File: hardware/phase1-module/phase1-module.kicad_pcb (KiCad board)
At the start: 4 copper layers, 120 x 80 mm, 144 parts, among them J1 VBUS IN, J2 SWD, J3 UART, J4 OUTPUT, J5 BACKPLANE, J6 FAN, Q1 CSD18563Q5A, Q2 CSD18563Q5A, Q3 60V NFET, Q4 60V NFET, Q5 2N7002, Q6 2N7002, Q7 2N7002, Q8 2N7002, Q9 2N7002, U1 DAC80502DRXT, U10 STM32G431CBT6, U11 TCAN1042HGV, U2 OPA2333, U3 LM5145RGYR, U4 INA240A3, U5 INA228, U6 LTC7004, U7 TLV7011, U8 LMR36015AQRNXRQ1, U9 NCP1117-3.3, Y1 8MHz

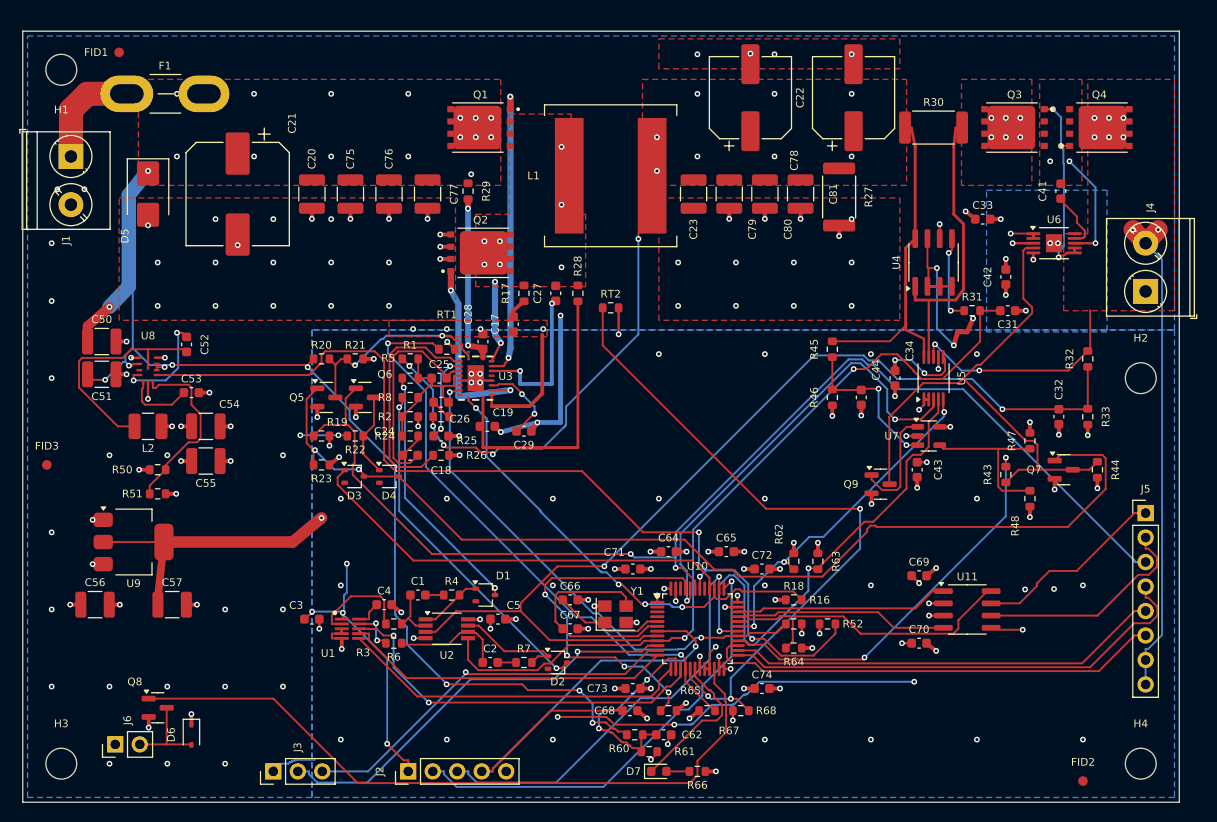
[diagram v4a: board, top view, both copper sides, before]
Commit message: Phase-1 100x80 (WIP): re-place output section around the 17 mm L1 land
Placement, pours and pass-1 copper for the 100 x 80 board; routing to follow.
Also corrects the Phase-1 F1 BOM note (direct-solder mini blade land).

Co-Authored-By: Claude Opus 5.5 (1M context) <noreply@anthropic.com>
Claude-Session: https://claude.ai/code/session_017ZrT5TjsLMQoxTZy1jabew
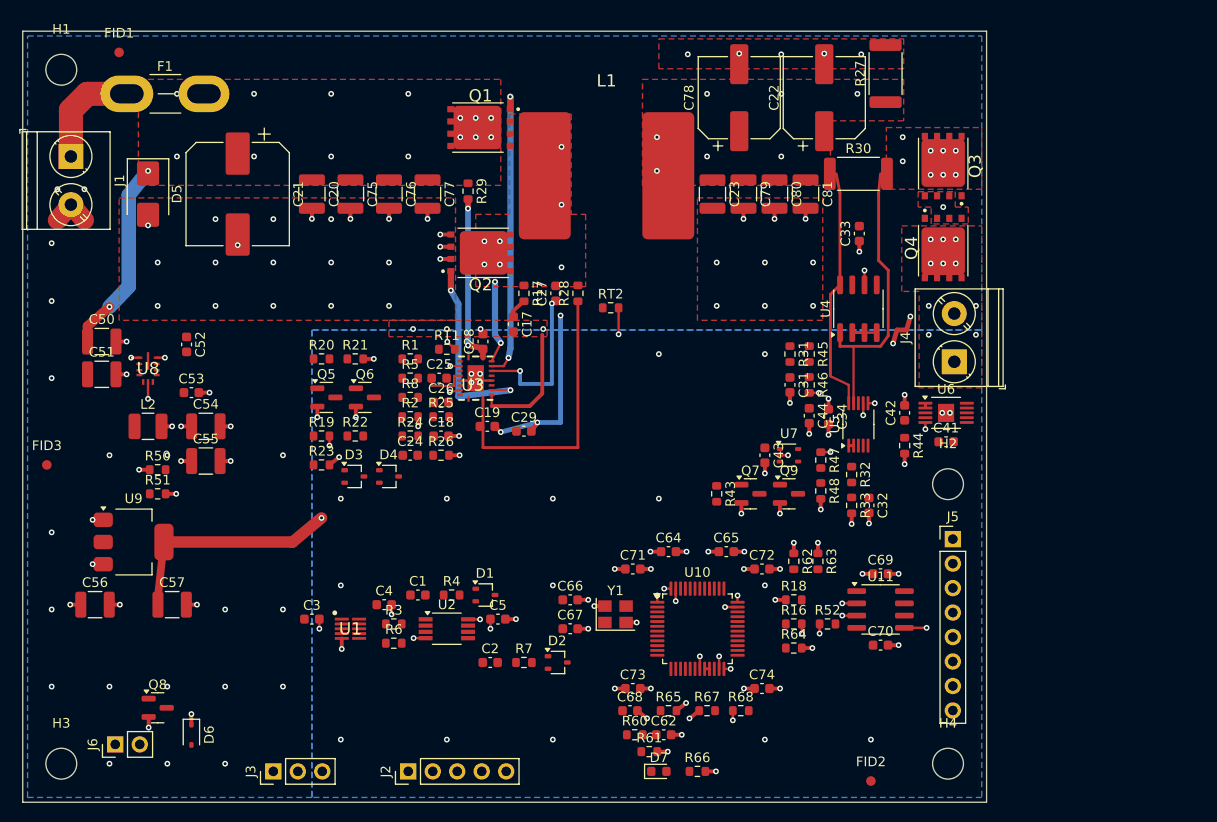
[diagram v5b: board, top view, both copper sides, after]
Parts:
- C1, C17, C18, C19, C2, C24, C25, C26, C27, C28, C29, C3, C31, C32, C33, C34, C4, C41, C42, C43, C44, C5, C52, C53, C62, C64, C65, C68, C69, C70, C71, C72, C73, C74: footprint Capacitor_SMD:C_0603_1608Metric -> C_0603_1608Metric
- C20, C23, C50, C51, C54, C55, C56, C57, C75, C76, C77, C79, C80, C81: footprint Capacitor_SMD:C_1210_3225Metric -> C_1210_3225Metric
- C21: footprint Capacitor_SMD:CP_Elec_10x10.5 -> CP_Elec_10x10.5
- C22, C78: footprint Capacitor_SMD:CP_Elec_8x11.9 -> CP_Elec_8x11.9
- C66, C67: value 10p -> 18p; footprint Capacitor_SMD:C_0603_1608Metric -> C_0603_1608Metric
- D1, D2, D3, D4: footprint Package_TO_SOT_SMD:SOT-323_SC-70 -> SOT-323_SC-70
- D5: footprint Diode_SMD:D_SMB -> D_SMB
- D6: footprint Diode_SMD:D_SOD-323 -> D_SOD-323
- D7: footprint LED_SMD:LED_0603_1608Metric -> LED_0603_1608Metric
- F1: footprint Fuse:Fuse_Blade_Mini_directSolder -> Fuse_Blade_Mini_directSolder
- FID1, FID2, FID3: footprint Fiducial:Fiducial_1mm_Mask2mm -> Fiducial_1mm_Mask2mm
- H1, H2, H3, H4: footprint MountingHole:MountingHole_3.2mm_M3 -> MountingHole_3.2mm_M3
- J1, J4: footprint TerminalBlock_Phoenix:TerminalBlock_Phoenix_PT-1,5-2-5.0-H_1x02_P5.00mm_Horizontal -> TerminalBlock_Phoenix_PT-1,5-2-5.0-H_1x02_P5.00mm_Horizontal
- J2: footprint Connector_PinHeader_2.54mm:PinHeader_1x05_P2.54mm_Vertical -> PinHeader_1x05_P2.54mm_Vertical
- J3: footprint Connector_PinHeader_2.54mm:PinHeader_1x03_P2.54mm_Vertical -> PinHeader_1x03_P2.54mm_Vertical
- J5: footprint Connector_PinHeader_2.54mm:PinHeader_1x08_P2.54mm_Vertical -> PinHeader_1x08_P2.54mm_Vertical
- J6: footprint Connector_PinHeader_2.54mm:PinHeader_1x02_P2.54mm_Vertical -> PinHeader_1x02_P2.54mm_Vertical
- L1: value XAL1350-103ME 10u/14A -> 10u MWSA1707S-100/XAL1350; footprint Inductor_SMD:L_Coilcraft_XAL1350-XXX -> L_1707_XAL1510
- L2: footprint Inductor_SMD:L_1210_3225Metric -> L_1210_3225Metric
- NT1: footprint NetTie:NetTie-2_SMD_Pad0.5mm -> NetTie-2_SMD_Pad0.5mm
- Q1, Q2, Q3, Q4: footprint labbench:PowerFET_SON5x6_GDS -> PowerFET_SON5x6_GDS
- Q5, Q6, Q7, Q8, Q9: footprint Package_TO_SOT_SMD:SOT-23 -> SOT-23
- R1, R16, R17, R18, R19, R2, R20, R21, R22, R23, R24, R25, R26, R28, R29, R3, R31, R32, R33, R4, R43, R44, R45, R46, R47, R48, R5, R50, R51, R52, R6, R60, R61, R62, R63, R64, R65, R66, R67, R68, R7, R8, RT1, RT2: footprint Resistor_SMD:R_0603_1608Metric -> R_0603_1608Metric
- R27, R30: footprint Resistor_SMD:R_2512_6332Metric -> R_2512_6332Metric
- U1: footprint labbench:DAC80502_DRX_WSON-10 -> DAC80502_DRX_WSON-10
- U10: footprint Package_QFP:LQFP-48_7x7mm_P0.5mm -> LQFP-48_7x7mm_P0.5mm
- U11, U4: footprint Package_SO:SOIC-8_3.9x4.9mm_P1.27mm -> SOIC-8_3.9x4.9mm_P1.27mm
- U2: footprint Package_SO:VSSOP-8_3.0x3.0mm_P0.65mm -> VSSOP-8_3.0x3.0mm_P0.65mm
- U3: footprint labbench:LM5145_RGY0020B -> LM5145_RGY0020B
- U5: footprint Package_SO:VSSOP-10_3x3mm_P0.5mm -> VSSOP-10_3x3mm_P0.5mm
- U6: footprint Package_SO:MSOP-10-1EP_3x3mm_P0.5mm_EP1.68x1.88mm -> MSOP-10-1EP_3x3mm_P0.5mm_EP1.68x1.88mm
- U7: value TLV7011 -> TLV7011DCK; footprint Package_TO_SOT_SMD:SOT-23-5 -> SOT-353_SC-70-5
- U8: footprint labbench:LMR36015_RNX_VQFN-HR-12 -> LMR36015_RNX_VQFN-HR-12
- U9: footprint Package_TO_SOT_SMD:SOT-223-3_TabPin2 -> SOT-223-3_TabPin2
- Y1: footprint Crystal:Crystal_SMD_3225-4Pin_3.2x2.5mm -> Crystal_SMD_3225-4Pin_3.2x2.5mm
- moved Q7 32.6 mm to (95.5, 68.0)
- moved R43 30.1 mm to (92.0, 68.0)
- moved C41 28.6 mm to (115.8, 62.6), turned to 0 degrees
- moved R32 27.3 mm to (106.0, 66.0)
- moved R33 26.2 mm to (106.0, 69.2)
- moved C31 23.9 mm to (99.6, 56.7), turned to -90 degrees
- moved H2 22.8 mm to (116.0, 67.0)
- moved FID2 22.0 mm to (108.0, 97.8)
- moved R47 21.8 mm to (102.8, 64.5)
- moved C32 21.7 mm to (107.8, 69.2)
- moved R48 21.7 mm to (102.8, 67.7)
- moved J4 21.1 mm to (116.7, 54.3)
- moved U6 20.9 mm to (115.8, 59.6)
- moved Q4 20.5 mm to (115.5, 42.5), turned to 90 degrees
- moved J5 20.2 mm to (116.5, 72.7)
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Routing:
- net HW_EN: track 122.9 -> 0.00 mm, vias 2 -> 0
- net EN_KILL: track 109.4 -> 0.00 mm, vias 2 -> 0
- net V_MEAS: track 103.4 -> 0.00 mm, vias 2 -> 0
- net AUX_PG: track 100.1 -> 0.00 mm, vias 3 -> 0
- net VBUS_F: track 117.4 -> 20.2 mm, vias 25 -> 16
- net I_MEAS: track 83.5 -> 0.00 mm, vias 2 -> 0
- net FAN_PWM: track 73.7 -> 0.00 mm
- net NTC_IND: track 71.3 -> 0.00 mm, vias 3 -> 0
- net NTC_FET: track 61.8 -> 0.00 mm, vias 2 -> 0
- net DISC_INP: track 57.8 -> 0.00 mm
- net VOUT_INT: track 82.5 -> 25.5 mm, vias 13 -> 7
- net I2C_SDA: track 52.1 -> 0.00 mm, vias 2 -> 0
- net PS_FPWM: track 52.8 -> 1.07 mm, vias 2 -> 1
- net NRST: track 50.2 -> 0.00 mm, vias 1 -> 0
- net SLOT_ID0: track 50.0 -> 0.00 mm
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- removed copper zone on In2.Cu, net DISC_SRC
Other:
- board size 120 x 80 mm -> 100 x 80 mm

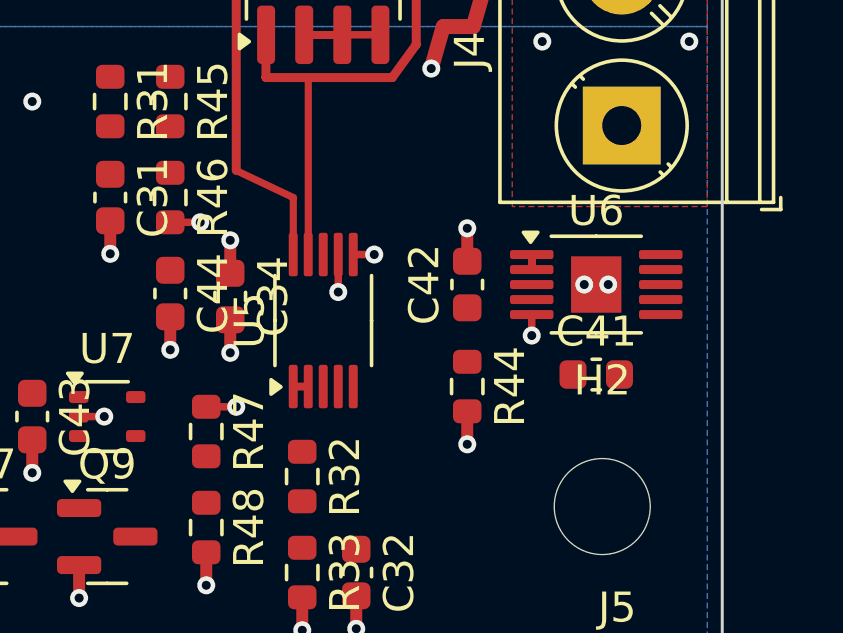
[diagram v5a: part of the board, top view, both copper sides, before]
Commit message: Phase-1 100x80 (WIP): turn U6 so gate/source/BST pins face their parts
Co-Authored-By: Claude Opus 5.5 (1M context) <noreply@anthropic.com>
Claude-Session: https://claude.ai/code/session_017ZrT5TjsLMQoxTZy1jabew
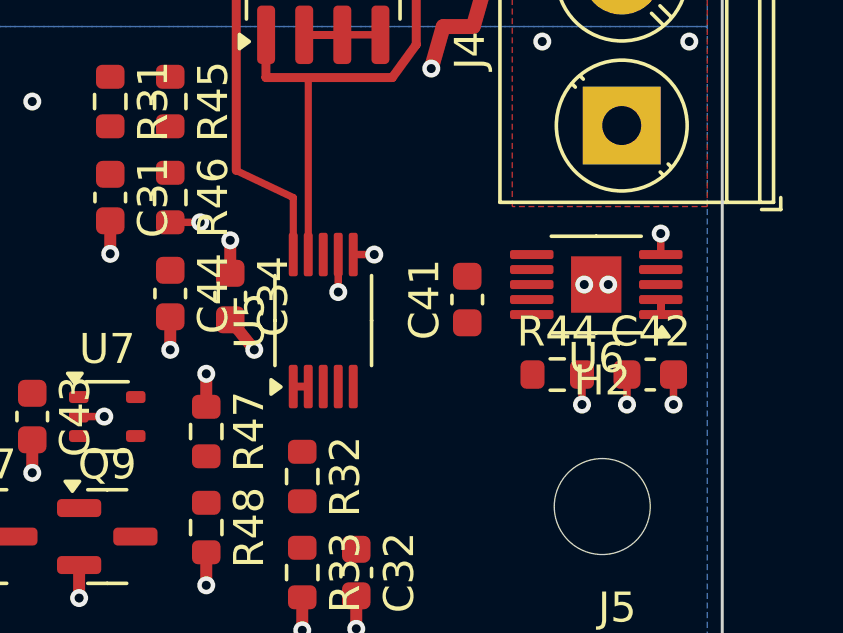
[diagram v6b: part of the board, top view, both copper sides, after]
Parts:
- moved C42 6.80 mm to (117.6, 62.6), turned to 0 degrees
- moved C41 4.97 mm to (111.5, 60.1), turned to 90 degrees
- moved R44 3.03 mm to (114.5, 62.6), turned to 0 degrees
- turned U6 to 180 degrees
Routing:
- net 5V0: track 16.1 -> 17.1 mm, vias 13 -> 14

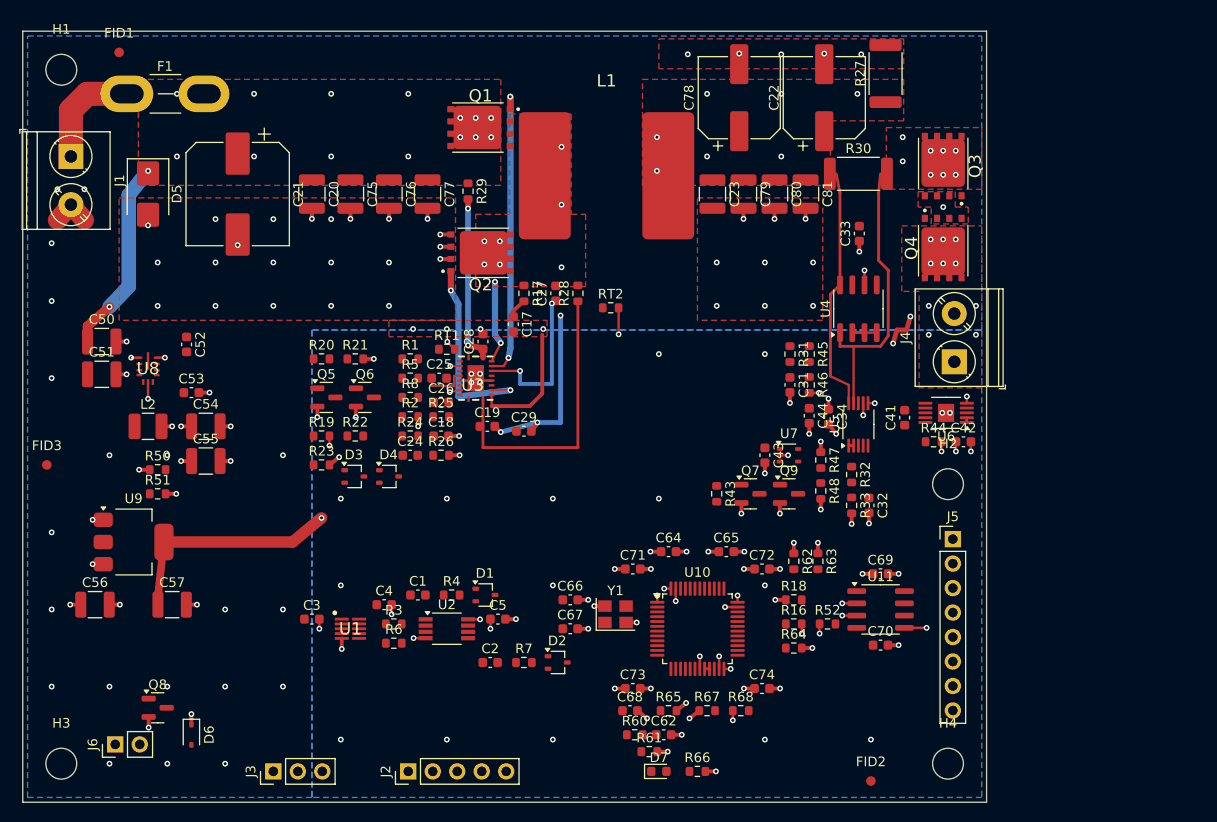
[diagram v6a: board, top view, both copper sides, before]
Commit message: Phase-1 board: 100 x 80 mm, re-routed with the BOM's L1 and U7 lands
Shrinks the module from 120 x 80 to 100 x 80 mm for JLCPCB's <=100 x 100
tier. The 120 x 80 layout stays on branch phase1-120x80.

- Re-placed from the netlist, so L1 gets the 17 mm MWSA1707S/XAL1510
  superset land and U7 the SC-70-5 land the BOM orders (the old board had
  XAL1350 and SOT-23-5 lands).
- Output bank tightened round L1; R27 moved to the top strip.
- R30, U4, U5 and the Kelvin pair moved as one block, same geometry.
- Q3/Q4, J4 and the LTC7004 stack down the right edge; U6 now below the
  seam, so the AGND pocket is gone.
- gen_board checks real courtyard polygons, not bounding boxes.
- Routed: 0 unconnected, 0 DRC errors, 11 silk warnings. Fab zip, CPL
  and BOM regenerated; F1 BOM note corrected (direct-solder mini blade).

Co-Authored-By: Claude Opus 5.5 (1M context) <noreply@anthropic.com>
Claude-Session: https://claude.ai/code/session_017ZrT5TjsLMQoxTZy1jabew
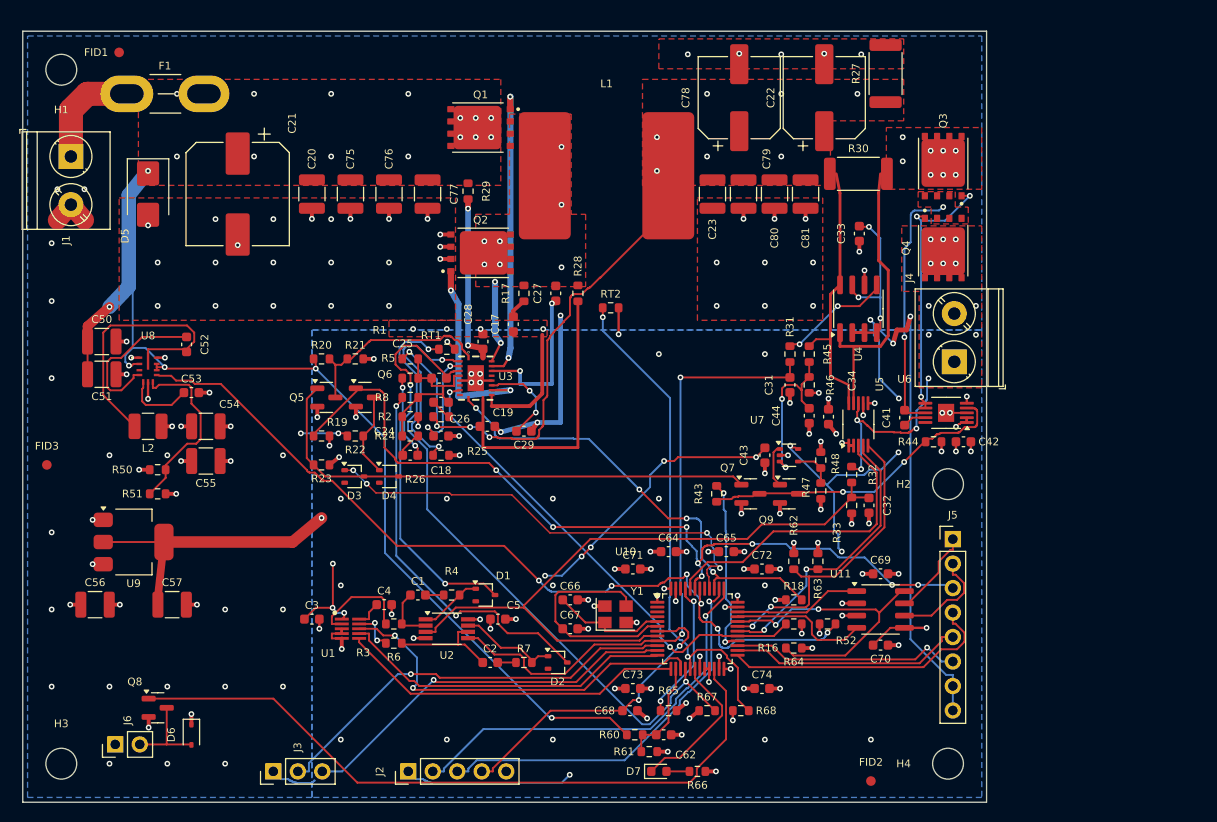
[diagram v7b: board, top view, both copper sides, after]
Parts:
- C1, C17, C18, C19, C2, C24, C25, C26, C27, C28, C29, C3, C31, C32, C33, C34, C4, C41, C42, C43, C44, C5, C52, C53, C62, C64, C65, C66, C67, C68, C69, C70, C71, C72, C73, C74: footprint C_0603_1608Metric -> Capacitor_SMD:C_0603_1608Metric
- C20, C23, C50, C51, C54, C55, C56, C57, C75, C76, C77, C79, C80, C81: footprint C_1210_3225Metric -> Capacitor_SMD:C_1210_3225Metric
- C21: footprint CP_Elec_10x10.5 -> Capacitor_SMD:CP_Elec_10x10.5
- C22, C78: footprint CP_Elec_8x11.9 -> Capacitor_SMD:CP_Elec_8x11.9
- D1, D2, D3, D4: footprint SOT-323_SC-70 -> Package_TO_SOT_SMD:SOT-323_SC-70
- D5: footprint D_SMB -> Diode_SMD:D_SMB
- D6: footprint D_SOD-323 -> Diode_SMD:D_SOD-323
- D7: footprint LED_0603_1608Metric -> LED_SMD:LED_0603_1608Metric
- F1: footprint Fuse_Blade_Mini_directSolder -> Fuse:Fuse_Blade_Mini_directSolder
- FID1, FID2, FID3: footprint Fiducial_1mm_Mask2mm -> Fiducial:Fiducial_1mm_Mask2mm
- H1, H2, H3, H4: footprint MountingHole_3.2mm_M3 -> MountingHole:MountingHole_3.2mm_M3
- J1, J4: footprint TerminalBlock_Phoenix_PT-1,5-2-5.0-H_1x02_P5.00mm_Horizontal -> TerminalBlock_Phoenix:TerminalBlock_Phoenix_PT-1,5-2-5.0-H_1x02_P5.00mm_Horizontal
- J2: footprint PinHeader_1x05_P2.54mm_Vertical -> Connector_PinHeader_2.54mm:PinHeader_1x05_P2.54mm_Vertical
- J3: footprint PinHeader_1x03_P2.54mm_Vertical -> Connector_PinHeader_2.54mm:PinHeader_1x03_P2.54mm_Vertical
- J5: footprint PinHeader_1x08_P2.54mm_Vertical -> Connector_PinHeader_2.54mm:PinHeader_1x08_P2.54mm_Vertical
- J6: footprint PinHeader_1x02_P2.54mm_Vertical -> Connector_PinHeader_2.54mm:PinHeader_1x02_P2.54mm_Vertical
- L1: footprint L_1707_XAL1510 -> labbench:L_1707_XAL1510
- L2: footprint L_1210_3225Metric -> Inductor_SMD:L_1210_3225Metric
- NT1: footprint NetTie-2_SMD_Pad0.5mm -> NetTie:NetTie-2_SMD_Pad0.5mm
- Q1, Q2, Q3, Q4: footprint PowerFET_SON5x6_GDS -> labbench:PowerFET_SON5x6_GDS
- Q5, Q6, Q7, Q8, Q9: footprint SOT-23 -> Package_TO_SOT_SMD:SOT-23
- R1, R16, R17, R18, R19, R2, R20, R21, R22, R23, R24, R25, R26, R28, R29, R3, R31, R32, R33, R4, R43, R44, R45, R46, R47, R48, R5, R50, R51, R52, R6, R60, R61, R62, R63, R64, R65, R66, R67, R68, R7, R8, RT1, RT2: footprint R_0603_1608Metric -> Resistor_SMD:R_0603_1608Metric
- R27, R30: footprint R_2512_6332Metric -> Resistor_SMD:R_2512_6332Metric
- U1: footprint DAC80502_DRX_WSON-10 -> labbench:DAC80502_DRX_WSON-10
- U10: footprint LQFP-48_7x7mm_P0.5mm -> Package_QFP:LQFP-48_7x7mm_P0.5mm
- U11, U4: footprint SOIC-8_3.9x4.9mm_P1.27mm -> Package_SO:SOIC-8_3.9x4.9mm_P1.27mm
- U2: footprint VSSOP-8_3.0x3.0mm_P0.65mm -> Package_SO:VSSOP-8_3.0x3.0mm_P0.65mm
- U3: footprint LM5145_RGY0020B -> labbench:LM5145_RGY0020B
- U5: footprint VSSOP-10_3x3mm_P0.5mm -> Package_SO:VSSOP-10_3x3mm_P0.5mm
- U6: footprint MSOP-10-1EP_3x3mm_P0.5mm_EP1.68x1.88mm -> Package_SO:MSOP-10-1EP_3x3mm_P0.5mm_EP1.68x1.88mm
- U7: footprint SOT-353_SC-70-5 -> Package_TO_SOT_SMD:SOT-353_SC-70-5
- U8: footprint LMR36015_RNX_VQFN-HR-12 -> labbench:LMR36015_RNX_VQFN-HR-12
- U9: footprint SOT-223-3_TabPin2 -> Package_TO_SOT_SMD:SOT-223-3_TabPin2
- Y1: footprint Crystal_SMD_3225-4Pin_3.2x2.5mm -> Crystal:Crystal_SMD_3225-4Pin_3.2x2.5mm
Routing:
- net VBUS_F: track 20.2 -> 111.1 mm, vias 16 -> 20
- net AUX_PG: track 0.00 -> 88.0 mm, vias 0 -> 6
- net HW_EN: track 0.00 -> 84.4 mm, vias 0 -> 8
- net FAN_PWM: track 0.00 -> 73.6 mm
- net V_MEAS: track 0.00 -> 69.2 mm
- net NTC_FET: track 0.00 -> 67.3 mm, vias 0 -> 2
- net I_MEAS: track 0.00 -> 65.6 mm, vias 0 -> 2
- net 5V0: track 17.1 -> 82.2 mm, vias 14 -> 27
- net EN_KILL: track 0.00 -> 53.9 mm
- net NTC_IND: track 0.00 -> 52.6 mm, vias 0 -> 2
- net VOUT_INT: track 25.5 -> 76.0 mm, vias 7 -> 11
- net PS_FPWM: track 1.07 -> 50.5 mm, vias 1 -> 2
- net PS_PGOOD: track 0.00 -> 47.3 mm, vias 0 -> 4
- net PS_OFF: track 0.00 -> 47.2 mm, vias 0 -> 4
- net UART_TX: track 0.00 -> 43.5 mm, vias 0 -> 1
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
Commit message: Phase-1: keep the FB sense run 5.5 mm from SW copper
Freerouting ran VOUT_INT's FB run 0.25 mm past the SW island. fb_reroute.py
rips it and re-routes with SW copper grown by 5.5 mm as a keep-out on every
layer: now 52 mm, >= 5.56 mm from SW. DRC unchanged (0 errors, 11 silk
warnings). Fab zip and CPL regenerated.

Co-Authored-By: Claude Opus 5.5 (1M context) <noreply@anthropic.com>
Claude-Session: https://claude.ai/code/session_017ZrT5TjsLMQoxTZy1jabew
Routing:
- net PGND: track 111.3 -> 106.9 mm
- net VOUT_INT: track 76.0 -> 80.3 mm, vias 11 -> 9
